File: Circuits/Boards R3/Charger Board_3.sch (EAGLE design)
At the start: 117 parts, among them CON1 ISP(2X3), CON13 HEADER_4X1, CON14 HEADER_3X1, CON15 HEADER_3X1, CON16 HEADER_4X1, CON17 HEADER_3X1, CON18 HEADER_3X1, CON19 HEADER_4X1, CON2 SCREWTERMINAL_1X2, CON20 HEADER_4X1, CON21 HEADER_4X1, CON22 HEADER_4X1, CON23 HEADER_4X1, CON24 HEADER_4X1, CON25 HEADER_4X1, CON26 HEADER_4X1, CON27 HEADER_4X1, CON28 HEADER_4X1, T1 IRLML6244TR, T2 IRLML6244TR, T3 SI4421DY, T4 IRLML6244TR, T5 IRLML6244TR, T6 IRLML6244TR, T7 IRLML6244TR, U1 ATMEGA324P, U2 ACS711, U3 JOYSTICKPTH, U4 MX25L25735E, U5 ATMEGA1281

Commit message: Both boards almost ready for routing
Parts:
- removed C10, C11: 12pf, Passive:CAP0603
- removed C3: 1uf, Passive:CAP0603
- removed CON18: HEADER_3X1, Mechanical:HEADER_3X1
- removed XTAL1: 10Mhz, Passive:NX5032GA-10.000000MHZ
- added C25: 1uf, Passive:CAP0603
- added CON3, CON4, CON5, CON6, CON7, CON8: HEADER_4X1, Mechanical:HEADER_4X1
- added R37, R38, R39, R40, R41, R42: 300, Passive:RES0603
- added R43: 10k, Passive:RES0603
- added U6: CD74HC154M96, DigitalIC:CD74HC154M96
- C24: value 1uf -> .1uf
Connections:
- removed net N$12: C10.1, U1.XTAL2, XTAL1.2
- removed net N$18: C14.2, S1.S, S1.S1
- removed net N$19: CON18.3, U1.PD3(PCINT27/TXD1/INT1)
- removed net N$25: C11.1, U1.XTAL1, XTAL1.1
- removed net N$4: CON18.2, U1.PD2(PCINT26/RXD1/INT0)
- removed net N$7: CON17.3, U1.PD1(PCINT25/TXD0)
- removed net N$8: CON17.2, U1.PD0(PCINT24/RXD0)
- removed net SCL: CON13.2, U1.PC0(PCINT16/SCL)
- removed net SDA: CON13.3, U1.PC1(PCINT17/SDA)
- removed net SECTION1: U1.PD4(PCINT28/XCK1/OC1B)
- removed net SECTION10: U1.PC7(TOSC2/PCINT23)
- removed net SECTION2: U1.PD5(PCINT29/OC1A)
- removed net SECTION3: U1.PD6(PCINT30/OC2B/ICP)
- removed net SECTION4: U1.PD7(PCINT31/OC2A)
- removed net SECTION5: U1.PC2(PCINT18/TCK)
- removed net SECTION6: U1.PC3(PCINT19/TMS)
- removed net SECTION7: U1.PC4(TDO/PCINT20)
- removed net SECTION8: U1.PC5(TDI/PCINT21)
- removed net SECTION9: U1.PC6(TOSC1/PCINT22)
- new net A0: U6.A0
- new net A1: U6.A1
- new net A2: U6.A2
- new net A3: U6.A3
- new net CTX: U5.PE1(TXD0/PDO), U6.!E1
- new net CTX11: CON3.3, U6.!Y10
- new net CTX12: CON4.3, U6.!Y11
- new net CTX13: CON5.3, U6.!Y12
- new net CTX14: CON6.3, U6.!Y13
- new net CTX15: CON7.3, U6.!Y14
- new net CTX16: CON8.3, U6.!Y15
- new net N$49: CON3.4, R37.2
- new net N$50: CON4.4, R38.2
- new net N$51: CON5.4, R39.2
- new net N$52: CON6.4, R40.2
- new net N$53: CON7.4, R41.2
- new net N$54: CON8.4, R42.2
- new net N$55: CON13.2, U5.PD0(SCL/INT0)
- new net N$56: CON13.3, U5.PD1(SDA/INT1)
- new net N$57: R43.1, U6.!E2
- new net N$60: CON17.2, U5.PD2(RXD1/INT2)
- new net N$61: CON17.3, U5.PD3(TXD1/INT3)
- net +3V: now also C25.1, U6.VCC; no longer C3.1, U1.AREF, U1.AVCC, U1.VCC
- net CHARGE+: now also CON3.2, CON4.2, CON5.2, CON6.2, CON7.2, CON8.2
- net CRX: now also R37.1, R38.1, R39.1, R40.1, R41.1, R42.1, U5.PE0(RXD0/PCINT8/PDI)
- net CTX1: now also U6.!Y0
- net CTX10: now also U6.!Y9
- net CTX2: now also U6.!Y1
- net CTX3: now also U6.!Y2
- net CTX4: now also U6.!Y3
- net CTX5: now also U6.!Y4
- net CTX6: now also U6.!Y5
- net CTX7: now also U6.!Y6
- net CTX8: now also U6.!Y7
- net CTX9: now also U6.!Y8
- net GND: now also C14.2, C25.2, CON3.1, CON4.1, CON5.1, CON6.1, CON7.1, CON8.1, R43.2, S1.S, S1.S1, U6.GND; no longer C10.2, C11.2, C3.2, CON18.1, U1.GND
- net MISO: no longer U1.PB6(PCINT14/MISO)
- net MOSI: no longer U1.PB5(PCINT13/MOSI)
- net RESET: no longer U1.!RESET
- net SCK: no longer U1.PB7(PCINT15/SCK)
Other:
- moved on the sheet: C1, C12, C14, C16, C17, C18, C19, C2, C20, C21, C22, C23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

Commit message: same as last
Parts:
- added TST1, TST2: TESTPOINT, Mechanical:TESTPOINT
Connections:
- new net DEBUG1: TST2.P$1
- new net DEBUG2: TST1.P$1
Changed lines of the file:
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@@
 <part name="GND24" library="Supply" deviceset="GND" device=""/>
 <part name="GND1" library="Supply" deviceset="GND" device=""/>
+<part name="TST1" library="Mechanical" deviceset="TESTPOINT" device=""/>
+<part name="TST2" library="Mechanical" deviceset="TESTPOINT" device=""/>
 </parts>
 <sheets>
@@
 <instance part="GND24" gate="1" x="289.56" y="-60.96"/>
 <instance part="GND1" gate="1" x="-124.46" y="-12.7"/>
+<instance part="TST1" gate="G$1" x="-106.68" y="-66.04" rot="R270"/>
+<instance part="TST2" gate="G$1" x="-119.38" y="-66.04" rot="R270"/>
 </instances>
 <busses>
@@
 <label x="226.06" y="-238.76" size="1.778" layer="91" xref="yes"/>
 </segment>
+<segment>
+<pinref part="TST2" gate="G$1" pin="P$1"/>
+<wire x1="-119.38" y1="-58.42" x2="-119.38" y2="-55.88" width="0.1524" layer="91"/>
+<label x="-119.38" y="-55.88" size="1.778" layer="91" rot="R90" xref="yes"/>
+</segment>
 </net>
 <net name="DEBUG2" class="0">
@@
 <label x="226.06" y="-241.3" size="1.778" layer="91" xref="yes"/>
 </segment>
-</net>
+<segment>
+<pinref part="TST1" gate="G$1" pin="P$1"/>
+<wire x1="-106.68" y1="-58.42" x2="-106.68" y2="-55.88" width="0.1524" layer="91"/>
+<label x="-106.68" y="-55.88" size="1.778" layer="91" rot="R90" xref="yes"/>
+</segment>
+</net>

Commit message: ready to route
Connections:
- new net LED6: R32.2
- new net LED7: R33.2
- net BUZZER: now also U5.PG5(OC0B)
- net LED4: now also R34.2, U5.PE5(OC3C/INT5); no longer R35.2
- net LED5: now also R35.2; no longer R33.2
- net MISO: no longer R32.2
- net MOSI: no longer R34.2
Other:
- moved on the sheet: CON13, LED11, LED12, LED8, LED9, R32, R33, R34, R35, U5
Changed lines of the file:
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@@
 <instance part="C2" gate="G$1" x="335.28" y="93.98"/>
 <instance part="C7" gate="G$1" x="342.9" y="93.98"/>
-<instance part="CON13" gate="G$1" x="-53.34" y="12.7" rot="MR0"/>
-<instance part="GND11" gate="1" x="-45.72" y="2.54" rot="MR0"/>
-<instance part="P+2" gate="1" x="-45.72" y="20.32" rot="MR0"/>
+<instance part="CON13" gate="G$1" x="116.84" y="30.48"/>
+<instance part="GND11" gate="1" x="109.22" y="20.32"/>
+<instance part="P+2" gate="1" x="109.22" y="38.1"/>
 <instance part="U3" gate="G$1" x="129.54" y="111.76"/>
 <instance part="GND13" gate="1" x="114.3" y="116.84" rot="R270"/>
@@
 <instance part="P+16" gate="1" x="114.3" y="101.6" rot="R90"/>
 <instance part="P+17" gate="1" x="185.42" y="71.12"/>
-<instance part="LED8" gate="G$1" x="-88.9" y="-40.64"/>
-<instance part="LED9" gate="G$1" x="-76.2" y="-40.64"/>
-<instance part="LED11" gate="G$1" x="-63.5" y="-40.64"/>
-<instance part="LED12" gate="G$1" x="-50.8" y="-40.64"/>
-<instance part="R32" gate="G$1" x="-88.9" y="-53.34" rot="R270"/>
-<instance part="R33" gate="G$1" x="-76.2" y="-53.34" rot="R270"/>
-<instance part="R34" gate="G$1" x="-63.5" y="-53.34" rot="R270"/>
-<instance part="R35" gate="G$1" x="-50.8" y="-53.34" rot="R270"/>
-<instance part="P+18" gate="1" x="-88.9" y="-27.94"/>
-<instance part="P+19" gate="1" x="-63.5" y="-27.94"/>
-<instance part="P+20" gate="1" x="-76.2" y="-27.94"/>
-<instance part="P+21" gate="1" x="-50.8" y="-27.94"/>
+<instance part="LED8" gate="G$1" x="-58.42" y="-43.18"/>
+<instance part="LED9" gate="G$1" x="-45.72" y="-43.18"/>
+<instance part="LED11" gate="G$1" x="-83.82" y="-43.18"/>
+<instance part="LED12" gate="G$1" x="-71.12" y="-43.18"/>
+<instance part="R32" gate="G$1" x="-58.42" y="-55.88" rot="R270"/>
+<instance part="R33" gate="G$1" x="-45.72" y="-55.88" rot="R270"/>
+<instance part="R34" gate="G$1" x="-83.82" y="-55.88" rot="R270"/>
+<instance part="R35" gate="G$1" x="-71.12" y="-55.88" rot="R270"/>
+<instance part="P+18" gate="1" x="-58.42" y="-30.48"/>
+<instance part="P+19" gate="1" x="-83.82" y="-30.48"/>
+<instance part="P+20" gate="1" x="-45.72" y="-30.48"/>
+<instance part="P+21" gate="1" x="-71.12" y="-30.48"/>
 <instance part="LED13" gate="G$1" x="45.72" y="88.9"/>
 <instance part="R36" gate="G$1" x="45.72" y="76.2" rot="R270"/>
@@
 <segment>
 <pinref part="CON13" gate="G$1" pin="4"/>
-<wire x1="-48.26" y1="7.62" x2="-45.72" y2="7.62" width="0.1524" layer="91"/>
-<wire x1="-45.72" y1="7.62" x2="-45.72" y2="5.08" width="0.1524" layer="91"/>
+<wire x1="111.76" y1="25.4" x2="109.22" y2="25.4" width="0.1524" layer="91"/>
+<wire x1="109.22" y1="25.4" x2="109.22" y2="22.86" width="0.1524" layer="91"/>
 <pinref part="GND11" gate="1" pin="GND"/>
 </segment>
@@
 <label x="226.06" y="-213.36" size="1.778" layer="91" xref="yes"/>
 </segment>
+<segment>
+<pinref part="U5" gate="G$1" pin="PG5(OC0B)"/>
+<wire x1="58.42" y1="-50.8" x2="60.96" y2="-50.8" width="0.1524" layer="91"/>
+<label x="60.96" y="-50.8" size="1.778" layer="91" xref="yes"/>
+</segment>
 </net>
 <net name="+5V" class="0">
@@
 <segment>
 <pinref part="CON13" gate="G$1" pin="1"/>
-<wire x1="-48.26" y1="15.24" x2="-45.72" y2="15.24" width="0.1524" layer="91"/>
-<wire x1="-45.72" y1="15.24" x2="-45.72" y2="17.78" width="0.1524" layer="91"/>
+<wire x1="111.76" y1="33.02" x2="109.22" y2="33.02" width="0.1524" layer="91"/>
+<wire x1="109.22" y1="33.02" x2="109.22" y2="35.56" width="0.1524" layer="91"/>
 <pinref part="P+2" gate="1" pin="+5V"/>
 </segment>
@@
 <label x="-22.86" y="30.48" size="1.778" layer="91" rot="R180" xref="yes"/>
 </segment>
-<segment>
-<pinref part="R34" gate="G$1" pin="2"/>
-<wire x1="-63.5" y1="-58.42" x2="-63.5" y2="-60.96" width="0.1524" layer="91"/>
-<label x="-63.5" y="-60.96" size="1.778" layer="91" rot="R270" xref="yes"/>
-</segment>
 </net>
 <net name="MISO" class="0">
@@
 <wire x1="-10.16" y1="27.94" x2="-33.02" y2="27.94" width="0.1524" layer="91"/>
 <label x="-33.02" y="27.94" size="1.778" layer="91" rot="R180" xref="yes"/>
-</segment>
-<segment>
-<pinref part="R32" gate="G$1" pin="2"/>
-<wire x1="-88.9" y1="-58.42" x2="-88.9" y2="-60.96" width="0.1524" layer="91"/>
-<label x="-88.9" y="-60.96" size="1.778" layer="91" rot="R270" xref="yes"/>
 </segment>
 </net>
@@
 <pinref part="P+18" gate="1" pin="+3V"/>
 <pinref part="LED8" gate="G$1" pin="A"/>
-<wire x1="-88.9" y1="-30.48" x2="-88.9" y2="-38.1" width="0.1524" layer="91"/>
+<wire x1="-58.42" y1="-33.02" x2="-58.42" y2="-40.64" width="0.1524" layer="91"/>
 </segment>
 <segment>
 <pinref part="P+20" gate="1" pin="+3V"/>
 <pinref part="LED9" gate="G$1" pin="A"/>
-<wire x1="-76.2" y1="-30.48" x2="-76.2" y2="-38.1" width="0.1524" layer="91"/>
+<wire x1="-45.72" y1="-33.02" x2="-45.72" y2="-40.64" width="0.1524" layer="91"/>
 </segment>
 <segment>
 <pinref part="P+19" gate="1" pin="+3V"/>
 <pinref part="LED11" gate="G$1" pin="A"/>
-<wire x1="-63.5" y1="-30.48" x2="-63.5" y2="-38.1" width="0.1524" layer="91"/>
+<wire x1="-83.82" y1="-33.02" x2="-83.82" y2="-40.64" width="0.1524" layer="91"/>
 </segment>
 <segment>
 <pinref part="P+21" gate="1" pin="+3V"/>
 <pinref part="LED12" gate="G$1" pin="A"/>
-<wire x1="-50.8" y1="-30.48" x2="-50.8" y2="-38.1" width="0.1524" layer="91"/>
+<wire x1="-71.12" y1="-33.02" x2="-71.12" y2="-40.64" width="0.1524" layer="91"/>
 </segment>
 <segment>
@@
 <pinref part="LED8" gate="G$1" pin="C"/>
 <pinref part="R32" gate="G$1" pin="1"/>
-<wire x1="-88.9" y1="-45.72" x2="-88.9" y2="-48.26" width="0.1524" layer="91"/>
+<wire x1="-58.42" y1="-48.26" x2="-58.42" y2="-50.8" width="0.1524" layer="91"/>
 </segment>
 </net>
@@
 <pinref part="LED9" gate="G$1" pin="C"/>
 <pinref part="R33" gate="G$1" pin="1"/>
-<wire x1="-76.2" y1="-45.72" x2="-76.2" y2="-48.26" width="0.1524" layer="91"/>
+<wire x1="-45.72" y1="-48.26" x2="-45.72" y2="-50.8" width="0.1524" layer="91"/>
 </segment>
 </net>
@@
 <pinref part="LED11" gate="G$1" pin="C"/>
 <pinref part="R34" gate="G$1" pin="1"/>
-<wire x1="-63.5" y1="-45.72" x2="-63.5" y2="-48.26" width="0.1524" layer="91"/>
+<wire x1="-83.82" y1="-48.26" x2="-83.82" y2="-50.8" width="0.1524" layer="91"/>
 </segment>
 </net>
@@
 <pinref part="LED12" gate="G$1" pin="C"/>
 <pinref part="R35" gate="G$1" pin="1"/>
-<wire x1="-50.8" y1="-45.72" x2="-50.8" y2="-48.26" width="0.1524" layer="91"/>
+<wire x1="-71.12" y1="-48.26" x2="-71.12" y2="-50.8" width="0.1524" layer="91"/>
 </segment>
 </net>
 <net name="LED5" class="0">
-<segment>
-<pinref part="R33" gate="G$1" pin="2"/>
-<wire x1="-76.2" y1="-58.42" x2="-76.2" y2="-60.96" width="0.1524" layer="91"/>
-<label x="-76.2" y="-60.96" size="1.778" layer="91" rot="R270" xref="yes"/>
-</segment>
 <segment>
 <wire x1="218.44" y1="-236.22" x2="226.06" y2="-236.22" width="0.1524" layer="91"/>
 <label x="226.06" y="-236.22" size="1.778" layer="91" xref="yes"/>
 </segment>
+<segment>
+<pinref part="R35" gate="G$1" pin="2"/>
+<wire x1="-71.12" y1="-60.96" x2="-71.12" y2="-63.5" width="0.1524" layer="91"/>
+<label x="-71.12" y="-63.5" size="1.778" layer="91" rot="R270" xref="yes"/>
+</segment>
 </net>
 <net name="LED4" class="0">
-<segment>
-<pinref part="R35" gate="G$1" pin="2"/>
-<wire x1="-50.8" y1="-58.42" x2="-50.8" y2="-60.96" width="0.1524" layer="91"/>
-<label x="-50.8" y="-60.96" size="1.778" layer="91" rot="R270" xref="yes"/>
-</segment>
 <segment>
 <wire x1="218.44" y1="-233.68" x2="226.06" y2="-233.68" width="0.1524" layer="91"/>
 <label x="226.06" y="-233.68" size="1.778" layer="91" xref="yes"/>
+</segment>
+<segment>
+<pinref part="U5" gate="G$1" pin="PE5(OC3C/INT5)"/>
+<wire x1="58.42" y1="-5.08" x2="60.96" y2="-5.08" width="0.1524" layer="91"/>
+<label x="60.96" y="-5.08" size="1.778" layer="91" xref="yes"/>
+</segment>
+<segment>
+<pinref part="R34" gate="G$1" pin="2"/>
+<wire x1="-83.82" y1="-60.96" x2="-83.82" y2="-63.5" width="0.1524" layer="91"/>
+<label x="-83.82" y="-63.5" size="1.778" layer="91" rot="R270" xref="yes"/>
 </segment>
 </net>
@@
 <pinref part="U5" gate="G$1" pin="PD0(SCL/INT0)"/>
 <pinref part="CON13" gate="G$1" pin="2"/>
-<wire x1="-10.16" y1="12.7" x2="-48.26" y2="12.7" width="0.1524" layer="91"/>
+<wire x1="58.42" y1="30.48" x2="111.76" y2="30.48" width="0.1524" layer="91"/>
 </segment>
 </net>
@@
 <pinref part="U5" gate="G$1" pin="PD1(SDA/INT1)"/>
 <pinref part="CON13" gate="G$1" pin="3"/>
-<wire x1="-10.16" y1="10.16" x2="-48.26" y2="10.16" width="0.1524" layer="91"/>
+<wire x1="58.42" y1="27.94" x2="111.76" y2="27.94" width="0.1524" layer="91"/>
 </segment>
 </net>
@@
 </segment>
 </net>
+<net name="LED6" class="0">
+<segment>
+<pinref part="R32" gate="G$1" pin="2"/>
+<wire x1="-58.42" y1="-60.96" x2="-58.42" y2="-63.5" width="0.1524" layer="91"/>
+<label x="-58.42" y="-63.5" size="1.778" layer="91" rot="R270" xref="yes"/>
+</segment>
+</net>
+<net name="LED7" class="0">
+<segment>
+<pinref part="R33" gate="G$1" pin="2"/>
+<wire x1="-45.72" y1="-60.96" x2="-45.72" y2="-63.5" width="0.1524" layer="91"/>
+<label x="-45.72" y="-63.5" size="1.778" layer="91" rot="R270" xref="yes"/>
+</segment>
+</net>

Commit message: both boards are routed
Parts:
- removed U1: ATMEGA324P, DigitalIC:ATMEGA324P
- R17, R18, R19, R2, R20, R3, R37, R38, R39, R4, R40, R41, R42, R5, R6, R9: value 300 -> 1k
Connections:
- net A0: now also U5.PB6(OC1B/PCINT6)
- net A1: now also U5.PB7(OC0A/OC1C/PCINT7)
- net A2: now also U5.PG3(TOSC2)
- net A3: now also U5.PG4(TOSC1)
- net BLUE: now also CON16.2; no longer CON16.1
- net BUTTON: no longer U1.PA3(ADC3/PCINT3)
- net BUZZER: no longer U1.PB4(!SS!/OC0B/PCINT12)
- net CHARGER: now also U5.PA7(AD7); no longer U1.PB0(XCK0/T0/PCINT8)
- net CS: now also U5.PE7(ICP3/CLKO/INT7); no longer U1.PA7(ADC7/PCINT7)
- net CURRENTSENSE: now also U5.PF2(ADC2); no longer U1.PA0(ADC0/PCINT0)
- net DEBUG1: now also U5.PG2(ALE)
- net DEBUG2: now also U5.PG0(!WR!)
- net GREEN: now also CON16.1; no longer CON16.2
- net HOLD: now also U5.PB5(OC1A/PCINT5); no longer U1.PA6(ADC6/PCINT6)
- net HORIZONTAL: now also U5.PF0(ADC0); no longer U1.PA2(ADC2/PCINT2)
- net LED1: now also U5.PC4(A12); no longer U1.PB1(T1/CLKO/PCINT9)
- net LED2: now also U5.PC3(A11); no longer U1.PB2(AIN0/INT2/PCINT10)
- net LED3: now also U5.PC2(A10); no longer U1.PB3(AIN1/OC0A/PCINT11)
- net LED5: now also U5.PG1(!RD!)
- net LED6: now also U5.PC0(A8)
- net LED7: now also U5.PA2(AD2)
- net TRANSMITLEDS: now also U5.PB0(!SS!/PCINT0); no longer U1.PA4(ADC4/PCINT4)
- net VERTICAL: now also U5.PF1(ADC1); no longer U1.PA1(ADC1/PCINT1)
- net WP: now also U5.PB4(OC2A/PCINT4); no longer U1.PA5(ADC5/PCINT5)

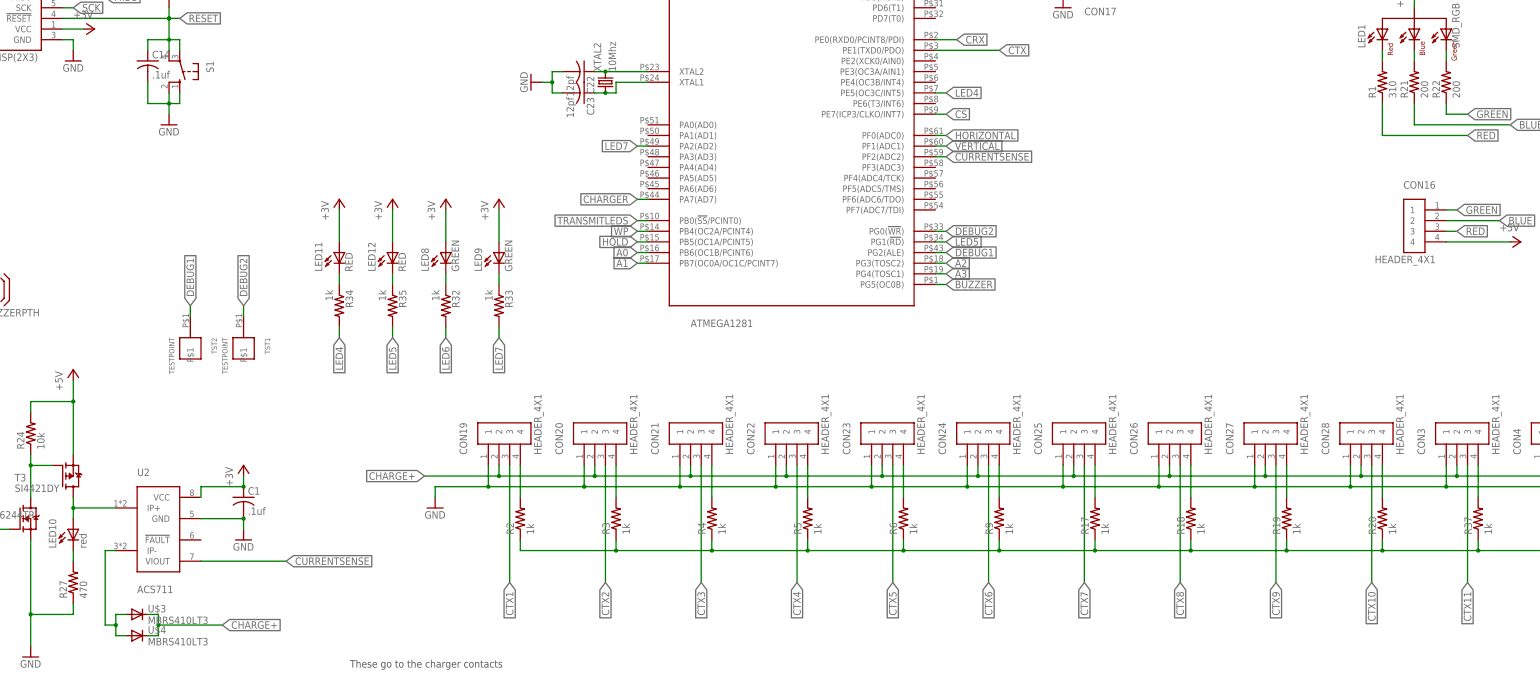
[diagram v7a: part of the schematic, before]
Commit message: BOMS and boards updated with a few slight value changes to reflect component availability
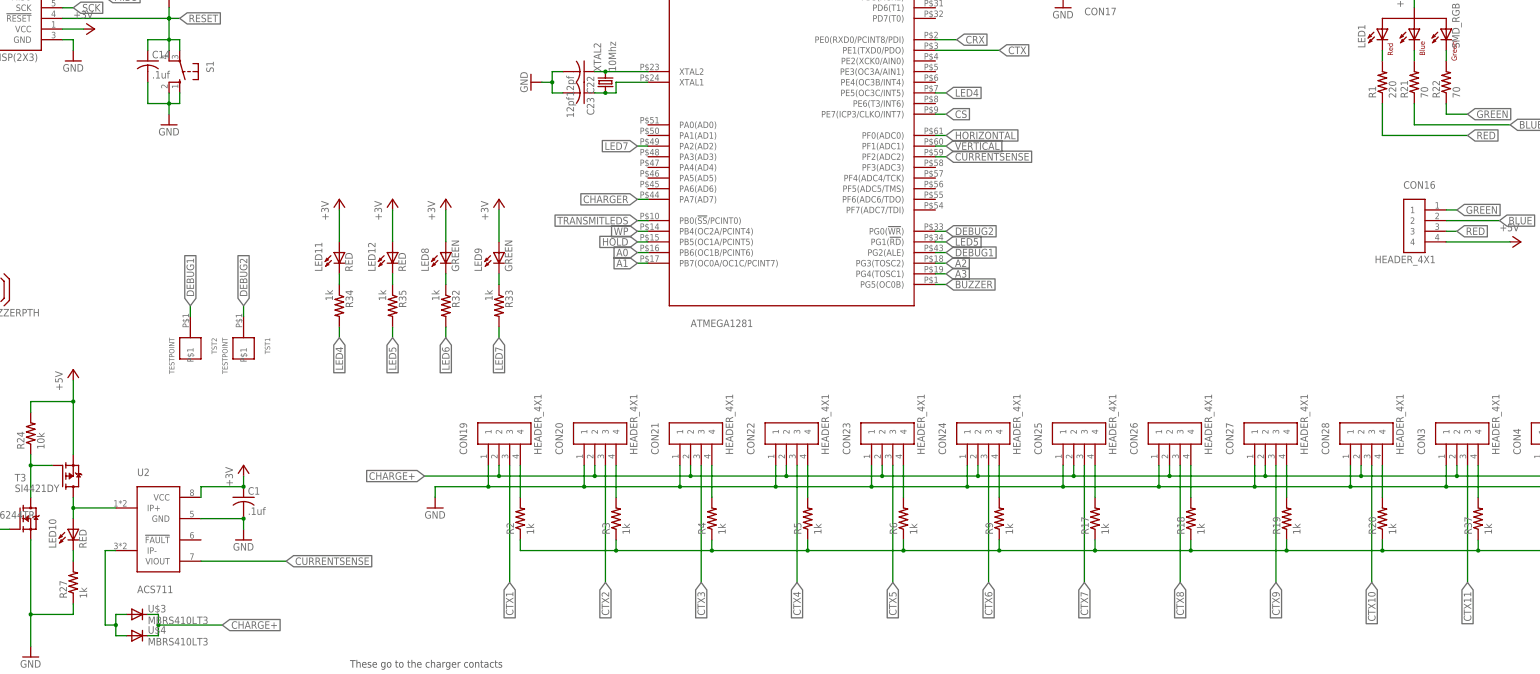
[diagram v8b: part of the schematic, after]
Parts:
- LED10: value red -> RED
- R1: value 310 -> 220
- R21, R22: value 200 -> 70
- R27: value 470 -> 1k
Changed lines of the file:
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@@
 <part name="LED6" library="Passive" deviceset="LED" device="5MMRA" value="IR"/>
 <part name="C6" library="Passive" deviceset="CAP" device="0805" value="10uf"/>
-<part name="LED10" library="Passive" deviceset="LED" device="0603" value="red"/>
-<part name="R27" library="Passive" deviceset="RES" device="0603" value="470"/>
+<part name="LED10" library="Passive" deviceset="LED" device="0603" value="RED"/>
+<part name="R27" library="Passive" deviceset="RES" device="0603" value="1k"/>
 <part name="R28" library="Passive" deviceset="RES" device="0603" value="1k"/>
 <part name="U2" library="PowerIC" deviceset="ACS711" device=""/>
@@
 <part name="GND12" library="Supply" deviceset="GND" device=""/>
 <part name="LED1" library="Passive" deviceset="SMD_RGB" device=""/>
-<part name="R1" library="Passive" deviceset="RES" device="0603" value="310"/>
-<part name="R21" library="Passive" deviceset="RES" device="0603" value="200"/>
-<part name="R22" library="Passive" deviceset="RES" device="0603" value="200"/>
+<part name="R1" library="Passive" deviceset="RES" device="0603" value="220"/>
+<part name="R21" library="Passive" deviceset="RES" device="0603" value="70"/>
+<part name="R22" library="Passive" deviceset="RES" device="0603" value="70"/>
 <part name="P+1" library="Supply" deviceset="+5V" device=""/>
 <part name="C2" library="Passive" deviceset="CAP" device="0603" value=".1uf"/>
